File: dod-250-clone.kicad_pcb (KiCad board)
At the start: 2 copper layers, 55 x 60 mm, 36 parts, among them U1 LM741

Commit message: Fix silkscreen on components
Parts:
- moved R5 1.00 mm to (27.0, 45.5)
- moved R4 0.50 mm to (28.5, 42.8)
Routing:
- net Net-(R5-Pad1): track 36.0 -> 37.0 mm
- net Net-(C4-Pad1): track 5.38 -> 6.38 mm
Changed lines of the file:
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@@
 		)
 		(property "Value" "100nF"
-			(at 2.5 2.5 90)
+			(at 1.5 -2.5 90)
 			(layer "F.SilkS")
 			(effects
@@
 		(tags "Resistor Axial_DIN0207 series Axial Horizontal pin pitch 7.62mm 0.25W = 1/4W length 6.3mm diameter 2.5mm")
 		(property "Reference" "R3"
-			(at 3.81 -2.37 0)
-			(layer "F.SilkS")
+			(at 7.31 2.5 0)
+			(layer "F.Fab")
 			(effects
 				(font
@@
 		)
 		(property "Value" "2.2MΩ"
-			(at 3.81 2.37 0)
-			(layer "F.Fab")
+			(at 3.81 -2.5 0)
+			(layer "F.SilkS")
 			(effects
 				(font
@@
 		)
 		(property "Value" "10pF"
-			(at 1.25 2.55 90)
+			(at 1.25 2.5 90)
 			(layer "F.SilkS")
 			(effects
@@
 	(footprint "Resistor_THT:R_Axial_DIN0207_L6.3mm_D2.5mm_P7.62mm_Horizontal"
 		(layer "F.Cu")
-		(at 26 45.5 -90)
+		(at 27 45.5 -90)
 		(descr "Resistor, Axial_DIN0207 series, Axial, Horizontal, pin pitch=7.62mm, 0.25W = 1/4W, length*diameter=6.3*2.5mm^2, http://cdn-reichelt.de/documents/datenblatt/B400/1_4W%23YAG.pdf")
 		(tags "Resistor Axial_DIN0207 series Axial Horizontal pin pitch 7.62mm 0.25W = 1/4W length 6.3mm diameter 2.5mm")
@@
 		(tags "Resistor Axial_DIN0207 series Axial Horizontal pin pitch 7.62mm 0.25W = 1/4W length 6.3mm diameter 2.5mm")
 		(property "Reference" "R2"
-			(at 3.81 -2.37 0)
-			(layer "F.SilkS")
+			(at 5.81 2.5 0)
+			(layer "F.Fab")
 			(effects
 				(font
@@
 		)
 		(property "Value" "10kΩ"
-			(at 3.81 2.37 0)
-			(layer "F.Fab")
+			(at 3.81 -2.5 0)
+			(layer "F.SilkS")
 			(effects
 				(font
@@
 		)
 		(property "Value" "1uF"
-			(at 2.5 2.5 0)
+			(at 4.5 2.5 0)
 			(layer "F.SilkS")
 			(effects
@@
 	(footprint "Resistor_THT:R_Axial_DIN0207_L6.3mm_D2.5mm_P7.62mm_Horizontal"
 		(layer "F.Cu")
-		(at 28 42.81 90)
+		(at 28.5 42.81 90)
 		(descr "Resistor, Axial_DIN0207 series, Axial, Horizontal, pin pitch=7.62mm, 0.25W = 1/4W, length*diameter=6.3*2.5mm^2, http://cdn-reichelt.de/documents/datenblatt/B400/1_4W%23YAG.pdf")
 		(tags "Resistor Axial_DIN0207 series Axial Horizontal pin pitch 7.62mm 0.25W = 1/4W length 6.3mm diameter 2.5mm")
@@
 		(layer "Edge.Cuts")
 	)
-	(gr_text "America's pedal for\n	America's 250th birthday"
-		(at 30.5 45 0)
+	(gr_text "America's pedal for\n   America's 250th birthday"
+		(at 31.5 45 0)
 		(layer "F.SilkS")
 		(effects
@@
 	)
 	(segment
-		(start 23.5 40.25)
-		(end 20.795 40.25)
-		(width 0.4064)
-		(layer "F.Cu")
-		(net 4)
-	)
-	(segment
-		(start 28 35.19)
-		(end 28 32.5)
+		(start 28.5 35.19)
+		(end 28.5 32)
 		(width 0.4064)
 		(layer "F.Cu")
@@
 	)
 	(segment
-		(start 28 32.5)
-		(end 28.5 32)
+		(start 23.5 40.25)
+		(end 20.795 40.25)
 		(width 0.4064)
 		(layer "F.Cu")
@@
 	)
 	(segment
-		(start 26.31 35.19)
-		(end 28 35.19)
+		(start 25.5 38.25)
+		(end 25.5 36)
 		(width 0.4064)
 		(layer "B.Cu")
@@
 	)
 	(segment
-		(start 25.5 38.25)
-		(end 25.5 36)
+		(start 25.5 36)
+		(end 26.31 35.19)
 		(width 0.4064)
 		(layer "B.Cu")
@@
 	)
 	(segment
-		(start 25.5 36)
-		(end 26.31 35.19)
+		(start 26.31 35.19)
+		(end 28.5 35.19)
 		(width 0.4064)
 		(layer "B.Cu")
@@
 	)
 	(segment
-		(start 23.88 51)
-		(end 26 53.12)
+		(start 24.88 51)
+		(end 27 53.12)
 		(width 0.4064)
 		(layer "F.Cu")
@@
 	(segment
 		(start 21.5 51)
-		(end 23.88 51)
+		(end 24.88 51)
 		(width 0.4064)
 		(layer "F.Cu")
@@
 	)
 	(segment
-		(start 26 45.5)
-		(end 23.771239 45.5)
+		(start 23.771239 45.5)
+		(end 27 45.5)
 		(width 0.4064)
 		(layer "B.Cu")

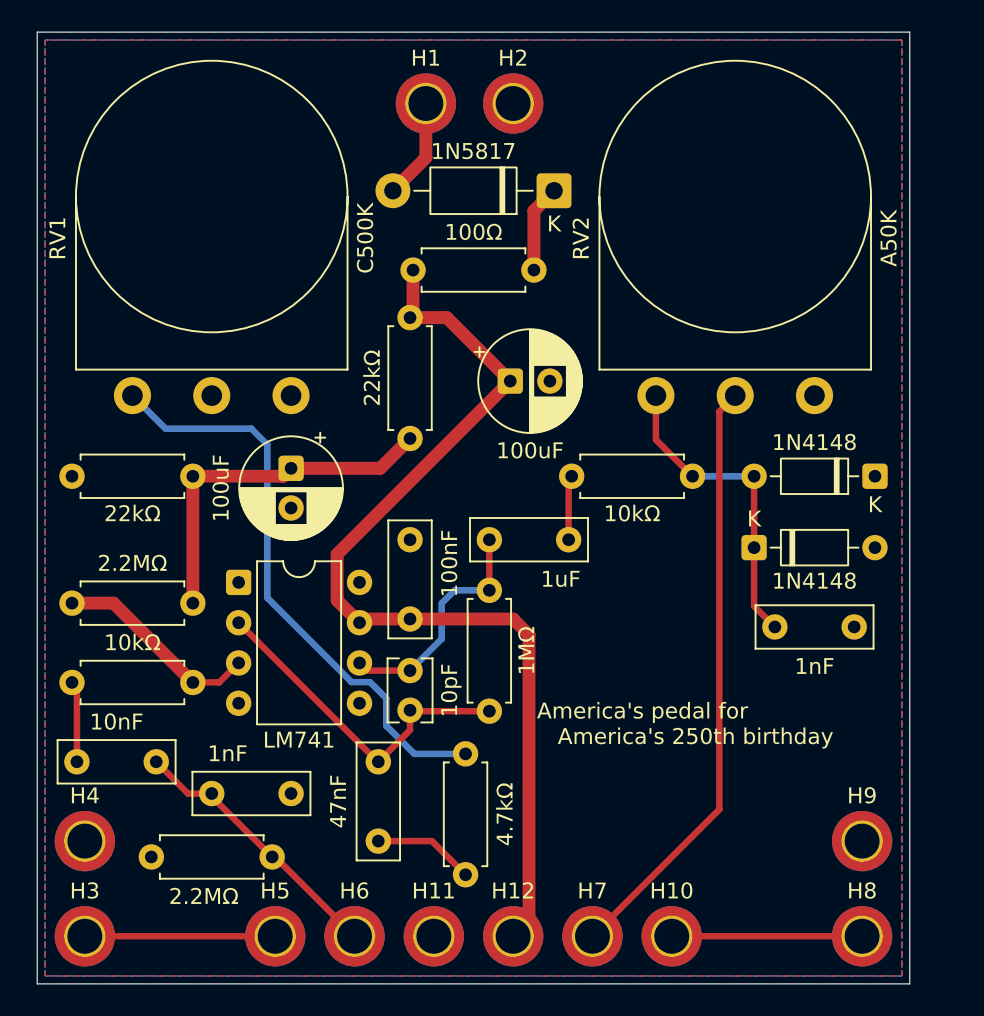
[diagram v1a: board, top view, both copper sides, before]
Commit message: Fix silkscreen for wire holes
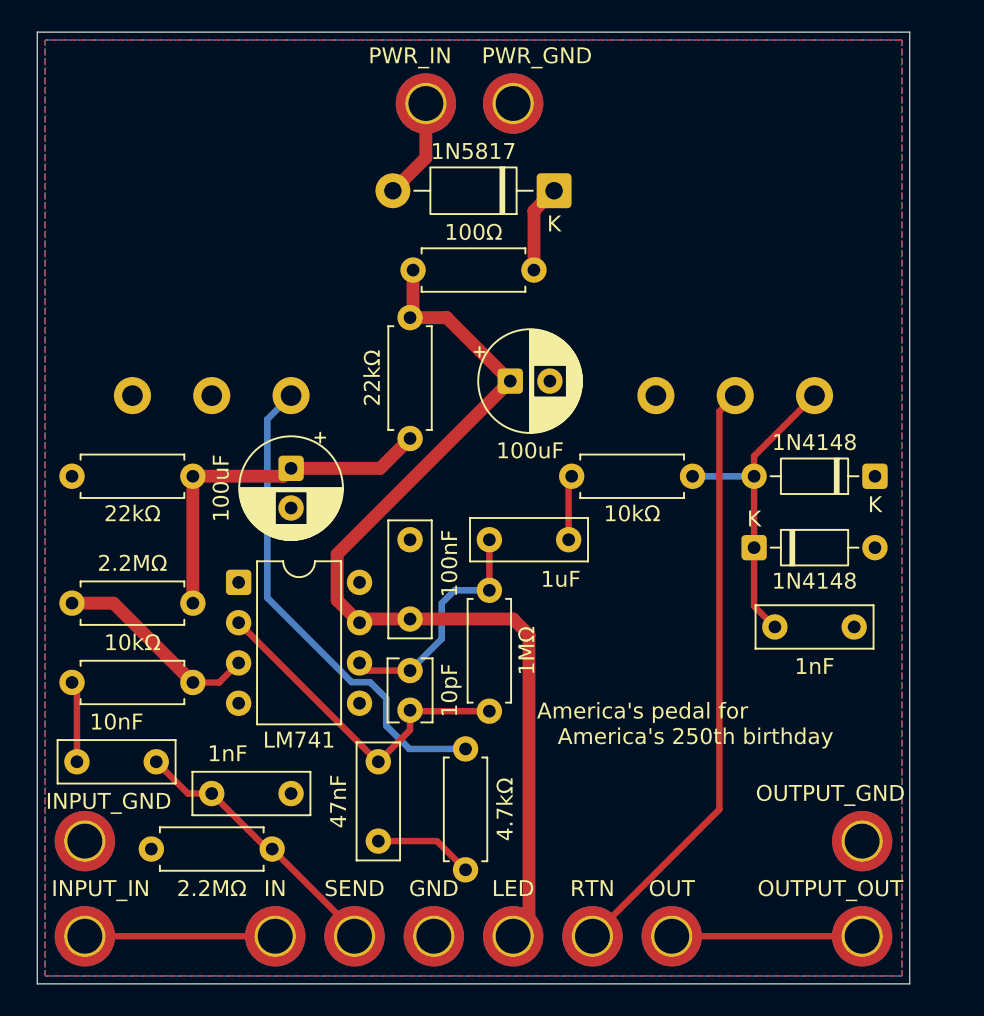
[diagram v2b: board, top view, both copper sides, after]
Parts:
- H10: value SW_OUT -> OUT
- H11: value SW_GND -> GND
- H12: value SW_LED -> LED
- H5: value SW_IN -> IN
- H6: value SW_SEND -> SEND
- H7: value SW_RTN -> RTN
- RV1, RV2: moved to B.Cu
- moved RV1 10.0 mm to (6.00, 22.9)
- moved RV2 10.0 mm to (39.0, 22.9)
- moved R1 0.50 mm to (14.8, 51.5)
- moved R5 0.31 mm to (27.0, 45.2)
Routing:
- net Net-(R5-Pad1): track 37.0 -> 30.8 mm
- net Net-(D1-A): track 20.0 -> 20.6 mm

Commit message: Fix pot footprints
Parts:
- RV1, RV2: footprint Potentiometer_THT:Potentiometer_Omeg_PC16BU_Vertical -> Floodlight_Custom_Footprints:Alpha_RV16AF-41
- moved RV1 16.7 mm to (11.0, 7.00), turned to 180 degrees
- moved RV2 16.7 mm to (44.0, 7.00), turned to 180 degrees
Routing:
- net Net-(R5-Pad1): track 30.8 -> 36.6 mm
- net Net-(D1-A): track 20.6 -> 19.9 mm

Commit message: Add Floodlight logo to PCB
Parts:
- added G***: LOGO, Floodlight_Custom_Footprints:floodlight_logo_vertical, F.Cu at (39.0, 36.5)
